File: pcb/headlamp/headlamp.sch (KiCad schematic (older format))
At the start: 57 parts, among them IC1 ATTINY841-SSU, P1 POWER, P2 SERIAL, P3 ISP, Q1 VEMT3700-GS08, Q2 NX2301P, Q3 DMP2035U, Q4 DMP2035U, SW1 BT2, SW2 BT1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

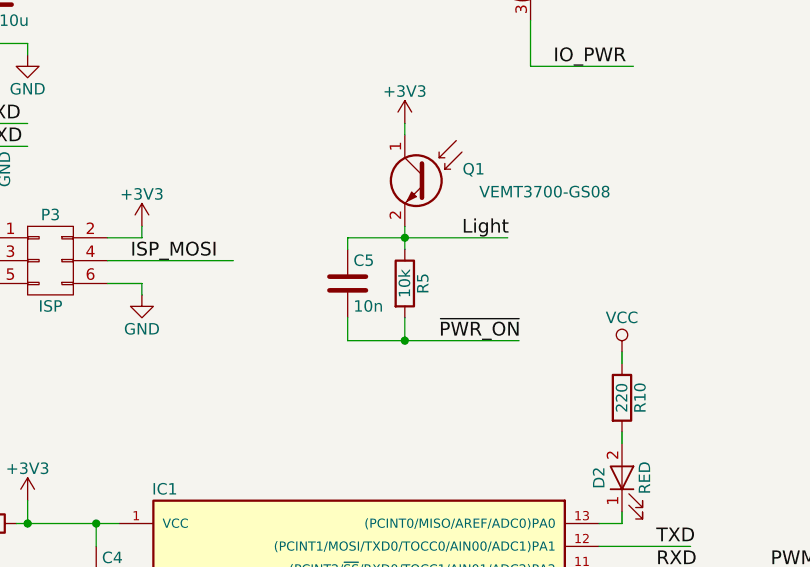
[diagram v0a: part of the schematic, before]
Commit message: Remove voltage spikes building up
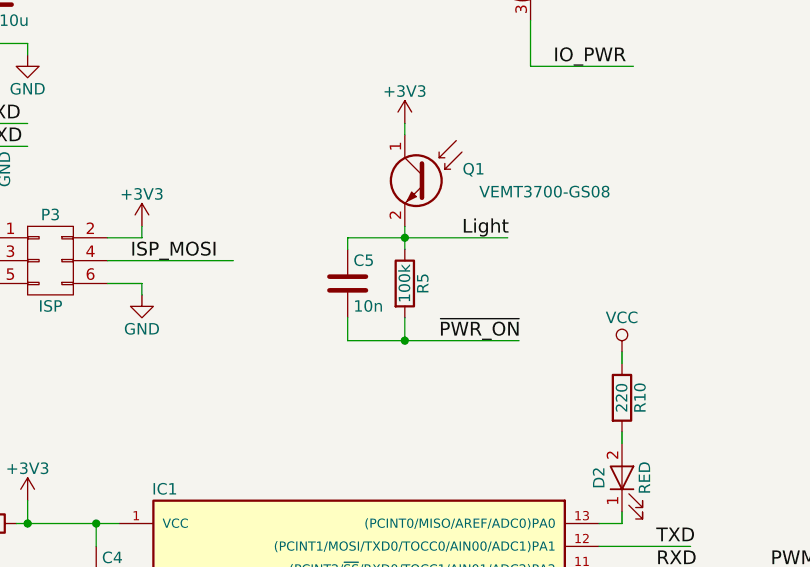
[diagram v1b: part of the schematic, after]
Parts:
- R5: value 10k -> 100k
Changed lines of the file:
@@
 Rev "0.2"
 Comp "Jakub Kaderka"
-Comment1 "3-4.2V input"
+Comment1 "3-4.2 V input"
 Comment2 "max 2A/LED"
-Comment3 "110-250kHz Switching frequency"
+Comment3 "250 kHz Switching frequency"
 Comment4 ""
 $EndDescr
@@
 P 2950 4450
 F 0 "R5" V 3030 4450 50  0000 C CNN
-F 1 "10k" V 2950 4450 50  0000 C CNN
+F 1 "100k" V 2950 4450 50  0000 C CNN
 F 2 "Resistors_SMD:R_0603" V 2880 4450 50  0001 C CNN
 F 3 "" H 2950 4450 50  0000 C CNN
